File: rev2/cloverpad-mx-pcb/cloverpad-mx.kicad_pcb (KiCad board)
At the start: 2 copper layers, 70 x 75 mm, 42 parts, among them J1 USB_C_Receptacle_USB2.0, SW1 SW_Push, SW2 SW_Push, U1 SRV05-4, U2 XC6206P332MR, U8 RP2040, U9 W25Q16JVSSIQ, Y1 12MHz

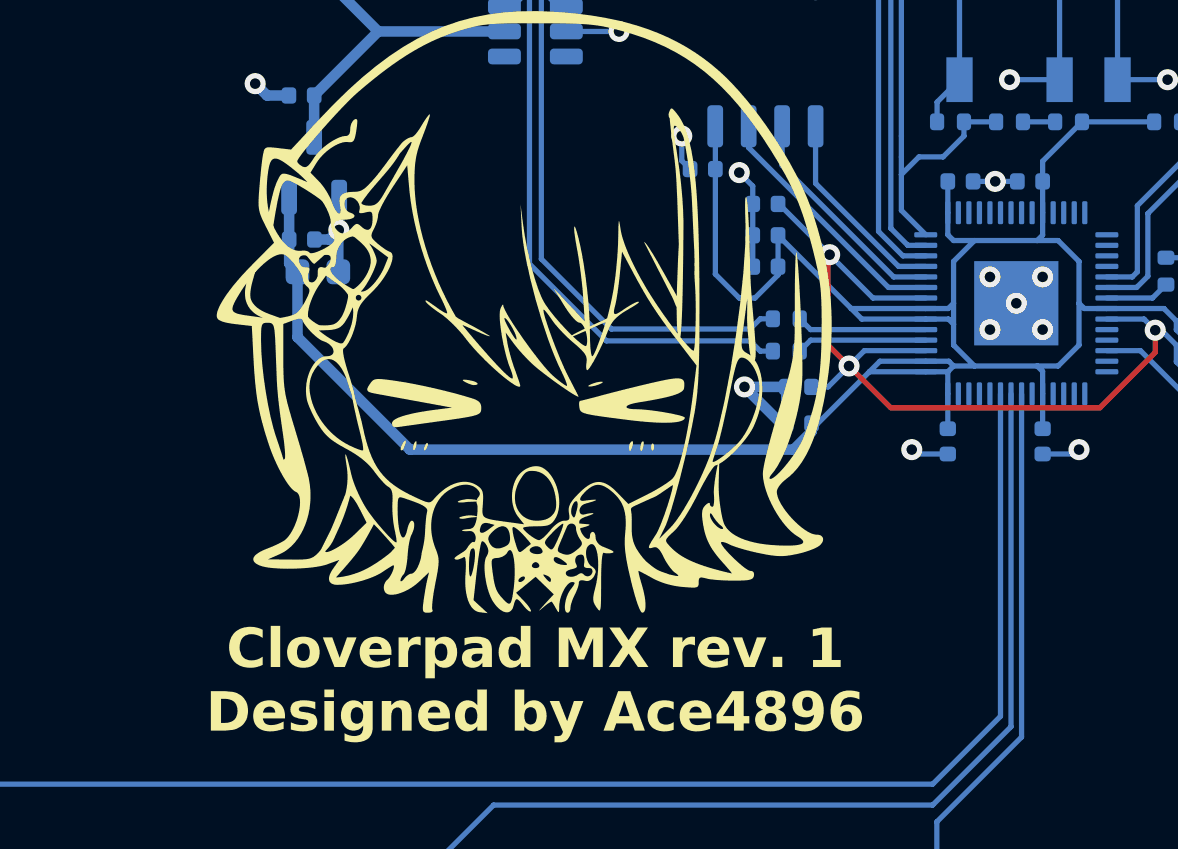
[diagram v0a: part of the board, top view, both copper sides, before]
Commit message: chore: update all symbols + footprints to match kicad 8
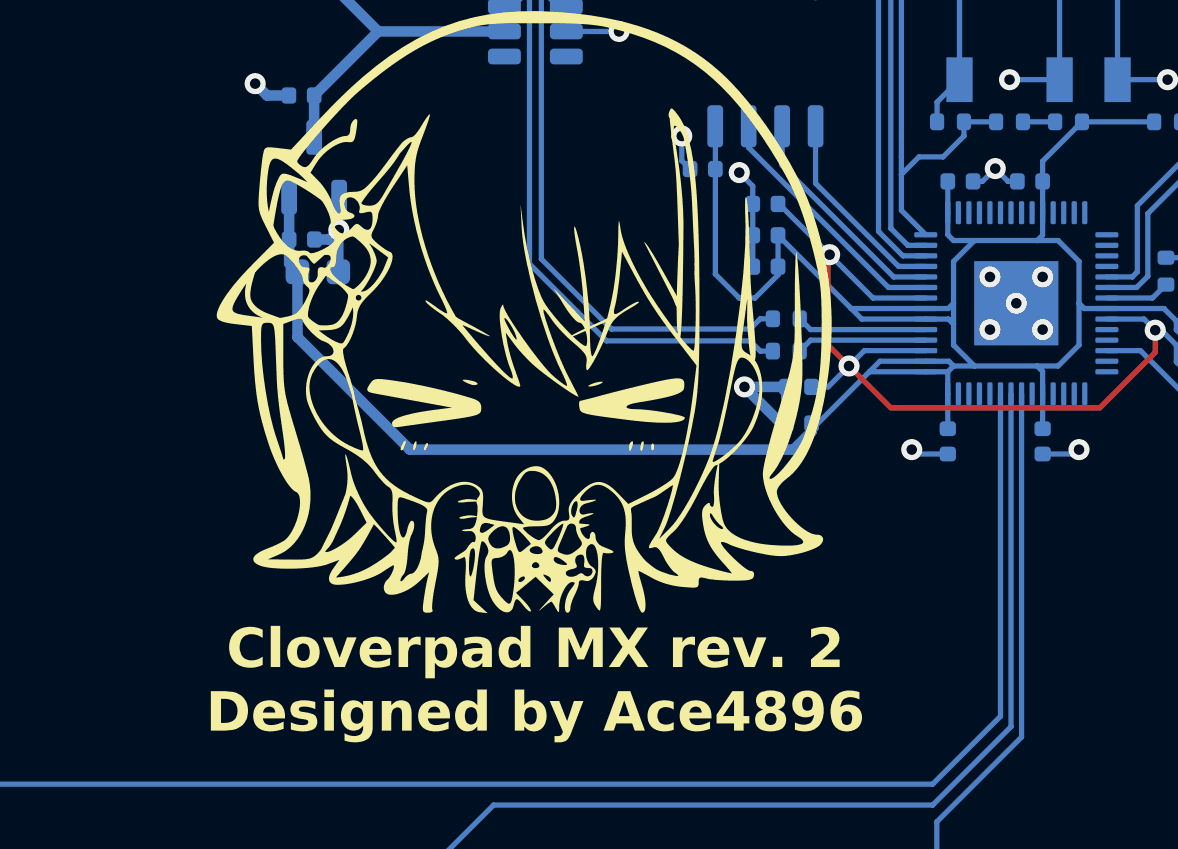
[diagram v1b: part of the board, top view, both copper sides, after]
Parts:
- MX1, MX2, MX3: footprint PCM_marbastlib-mx:SW_MX_HS_1u -> PCM_marbastlib-mx:SW_MX_HS_CPG151101S11_1u
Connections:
- J1 pad A8: unconnected-(J1-SBU1-PadA8) -> (no net)
- J1 pad B8: unconnected-(J1-SBU2-PadB8) -> (no net)
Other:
- board text added: "Cloverpad MX rev. 2 Designed by Ace4896"
- board text removed: "Cloverpad MX rev. 1 Designed by Ace4896"

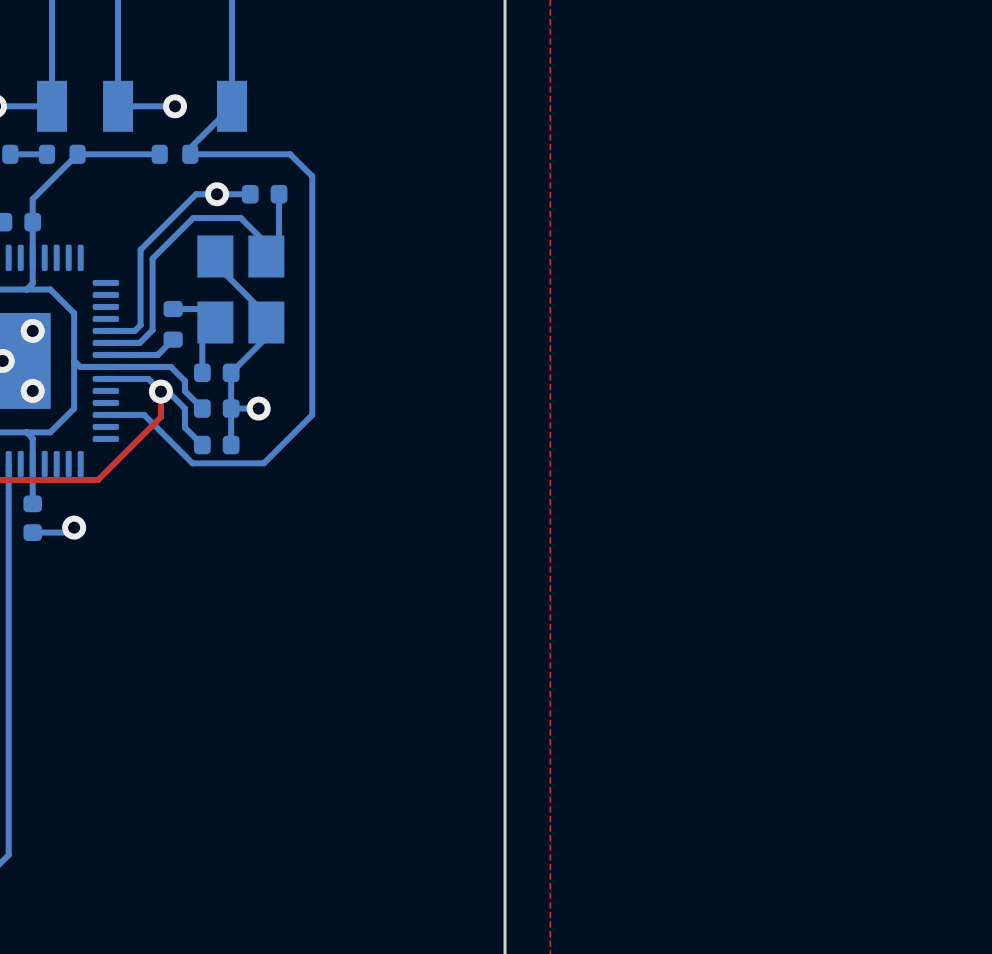
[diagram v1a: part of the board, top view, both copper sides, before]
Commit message: feat: new schematic for rev. 2, with various fixes and component changes
almost there - just need to figure out how to attach an EEPROM.
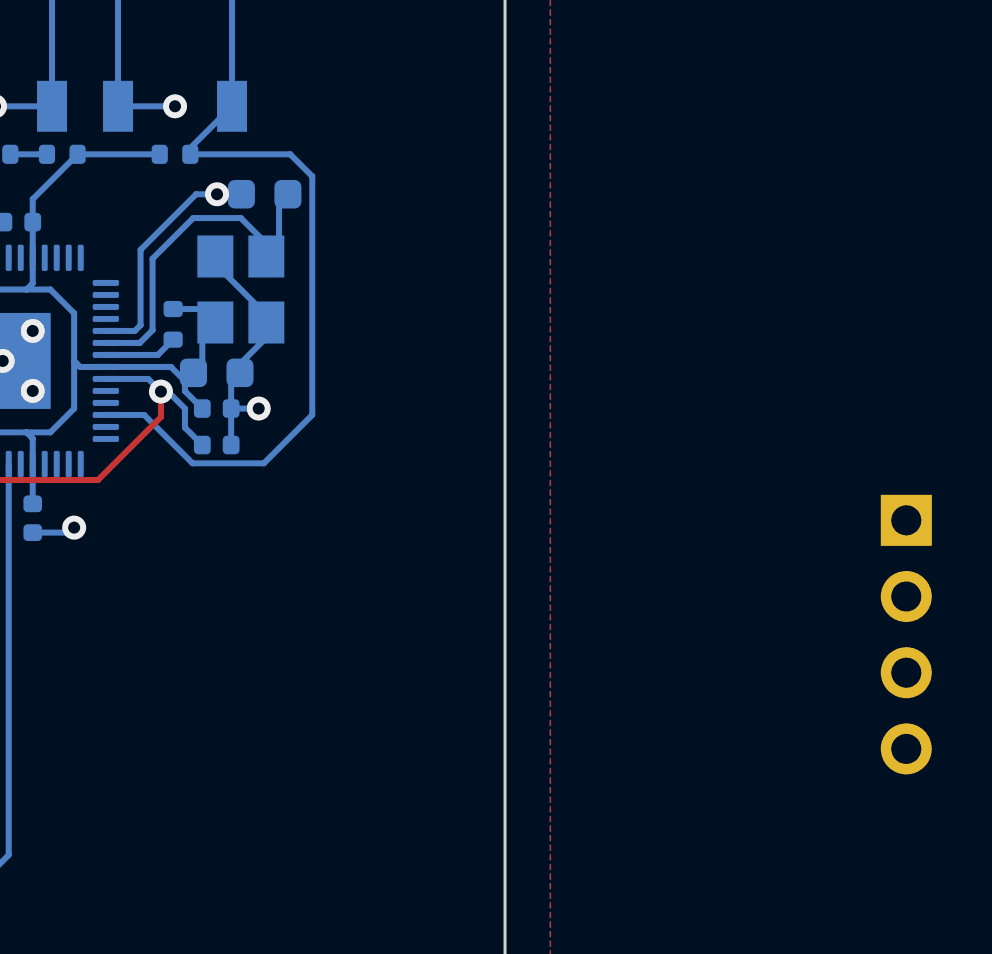
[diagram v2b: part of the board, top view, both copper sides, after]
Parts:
- added J2: Conn_01x04, Connector_PinHeader_2.54mm:PinHeader_1x04_P2.54mm_Horizontal, B.Cu at (106.2, 52.0)
- C15: renamed from C28; value 1uF -> 100nF
- C16: renamed from C24; value 22pF -> 30pF; footprint Capacitor_SMD:C_0402_1005Metric -> Capacitor_SMD:C_0603_1608Metric
- C17: renamed from C25; value 22pF -> 30pF; footprint Capacitor_SMD:C_0402_1005Metric -> Capacitor_SMD:C_0603_1608Metric
- R1, R2: value 5k1 -> 5.1k
- R5: renamed from R13; value 5k1 -> 10k (DNF)
- R7: renamed from R12; value 5k1 -> 1k
- U4: renamed from U9; value W25Q16JVSSIQ -> W25Q128JVS
- renumbered C4 to C1, C19 to C10, C20 to C11, C21 to C12, C22 to C13, C23 to C14, C5 to C2, C12 to C3, C13 to C4, C14 to C5, C15 to C6, C16 to C7, C17 to C8, C18 to C9, R9 to R3, R11 to R4, R14 to R6, R7 to R8, SW2 to SW1, SW1 to SW2, U2 to U1, U1 to U2, U8 to U3
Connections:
- net D+ renamed /USB_D+
- net D- renamed /USB_D-
- net Net-(U8-USB_DM) renamed /USB_DM
- net Net-(U8-USB_DP) renamed /USB_DP
- net Q_CLK renamed /QSPI_SCLK
- net Q_IO0 renamed /QSPI_SD0
- net Q_IO1 renamed /QSPI_SD1
- net Q_IO2 renamed /QSPI_SD2
- net Q_IO3 renamed /QSPI_SD3
- net Q_SEL renamed /QSPI_SS
- net RESET renamed /RUN
- net VBUS renamed Net-(F1-Pad2)
- net XIN renamed /XIN
- net XOUT renamed /XOUT
- J1 pad A8: (no net) -> unconnected-(J1-SBU1-PadA8)
- J1 pad B8: (no net) -> unconnected-(J1-SBU2-PadB8)
- MX1 pad 1: K1 -> /K1
- MX2 pad 1: K2 -> /K2
- MX3 pad 1: K3 -> /K3
- R5 pad 1: Net-(R10-Pad2) -> +3V3
- U3 pad 24: unconnected-(U8-SWCLK-Pad24) -> /SWCLK
- U3 pad 25: unconnected-(U8-SWD-Pad25) -> /SWD
- U3 pad 35: K3 -> unconnected-(U3-GPIO23-Pad35)
- U3 pad 36: K2 -> unconnected-(U3-GPIO24-Pad36)
- U3 pad 37: K1 -> unconnected-(U3-GPIO25-Pad37)
- U3 pad 38: unconnected-(U8-GPIO26_ADC0-Pad38) -> /K3
- U3 pad 39: unconnected-(U8-GPIO27_ADC1-Pad39) -> /K2
- U3 pad 40: unconnected-(U8-GPIO28_ADC2-Pad40) -> /K1
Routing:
- net K1: track 61.9 -> 0.00 mm
- net /K1: track 0.00 -> 61.9 mm
- net K2: track 43.0 -> 0.00 mm
- net /K2: track 0.00 -> 43.0 mm
- net K3: track 25.5 -> 0.00 mm
- net /K3: track 0.00 -> 25.5 mm
- net Net-(C25-Pad2): track 0.00 -> 3.45 mm
- net Net-(C17-Pad2): track 3.45 -> 0.00 mm
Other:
- board text added: "TODO: - Determine {dblquote}minimum{dblquote} PCB height (width is obvious, but height depends on routing) - Re-position components - Re-route all connections (components were re-labelled, so placement is wrong)"

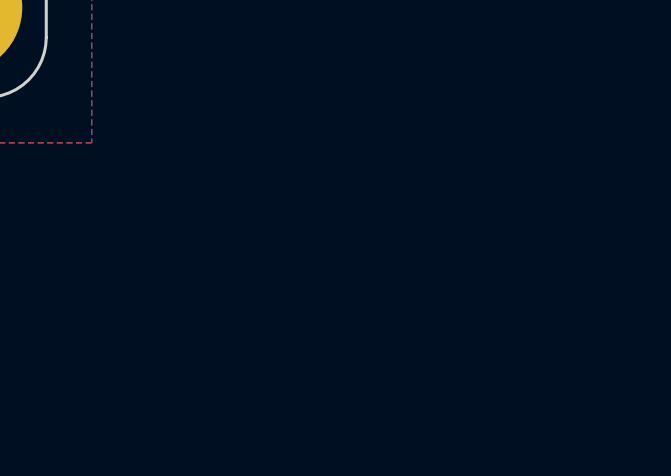
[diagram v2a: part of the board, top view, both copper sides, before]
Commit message: feat: add external AT24C32 EEPROM
for 3.3V, it seems that anything from 2k to 4.7k will work, but I've seen 10k working on Adafruit's EEPROM breakout. I've chosen 5.1k to minimise the BOM (the same ones used for USB).
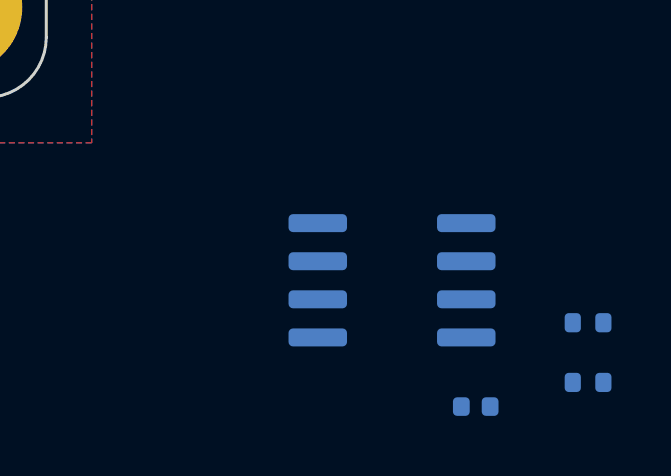
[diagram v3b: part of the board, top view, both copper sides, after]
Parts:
- added C16: 100nF, Capacitor_SMD:C_0402_1005Metric, B.Cu at (107.1, 103.1)
- added R3: 5k1, Resistor_SMD:R_0402_1005Metric, B.Cu at (110.9, 100.3)
- added R4: 5k1, Resistor_SMD:R_0402_1005Metric, B.Cu at (110.9, 102.3)
- added U4: AT24C32, Package_SO:SOIC-8_3.9x4.9mm_P1.27mm, B.Cu at (104.3, 98.9)
- R1, R2: value 5.1k -> 5k1
- renumbered C16 to C17, C17 to C18, R8 to R10, R3 to R5, R4 to R6, R6 to R8, R7 to R9, U4 to U5
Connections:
- U3 pad 2: unconnected-(U3-GPIO0-Pad2) -> /EEPROM_SDA
- U3 pad 3: unconnected-(U3-GPIO1-Pad3) -> /EEPROM_SCL
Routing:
- net Net-(C25-Pad2): track 3.45 -> 0.00 mm
- net +3V3: track 98.1 -> 101.6 mm
